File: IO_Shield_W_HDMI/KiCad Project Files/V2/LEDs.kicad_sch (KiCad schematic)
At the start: 70 parts, among them Q1 FDN340P, Q2 FDN340P, Q3 FDN340P, Q4 FDN340P, SW1 SW_DIP_x08, SW2 SW_DIP_x08

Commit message: working on placement
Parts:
- RN1, RN10, RN11, RN19, RN2, RN20, RN21, RN23, RN24, RN3, RN4, RN9: value R_Pack04 -> 1k
- RN13, RN14, RN15, RN16, RN17, RN22, RN7, RN8: value R_Pack04 -> 330
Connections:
- net AN2: no longer Q4.1 (G)
- net AFF0_B: now reaches RN7.8 (R1.2)
- net AFF0_B: now also AFF1.6 (b); no longer AFF1.1 (e)
- net AFF0_F: now reaches RN7.6 (R3.2)
- net AFF0_F: now also AFF1.9 (f); no longer AFF1.10 (g)
- net AFF0_D: now reaches AFF1.2 (d)
- net AFF0_D: now also RN5.7 (R2.2); no longer RN5.5 (R4.2)
- net AFF0_C: now reaches AFF1.4 (c), RN5.6 (R3.2)
- net AFF0_DP: now reaches AFF1.5 (DP)
- net AFF0_DP: now also RN5.5 (R4.2); no longer RN7.5 (R4.2)
- net AFF0_A: now reaches AFF1.7 (a)
- net AFF0_A: now also RN7.7 (R2.2); no longer RN5.8 (R1.2)
- net AFF1_B: now reaches RN8.8 (R1.2)
- net AFF1_B: now also AFF2.6 (b); no longer AFF2.1 (e)
- net AFF1_F: now reaches RN8.6 (R3.2)
- net AFF1_F: now also AFF2.9 (f); no longer AFF2.10 (g)
- net AFF1_D: now reaches AFF2.2 (d)
- net AFF1_D: now also RN6.7 (R2.2); no longer RN6.5 (R4.2)
- net AFF1_C: now reaches AFF2.4 (c), RN6.6 (R3.2)
- net AFF1_DP: now reaches AFF2.5 (DP)
- net AFF1_DP: now also RN6.5 (R4.2); no longer RN8.5 (R4.2)
- net AFF1_A: now reaches AFF2.7 (a)
- net AFF1_A: now also RN8.7 (R2.2); no longer RN6.8 (R1.2)
- net AFF2_B: now reaches RN13.8 (R1.2)
- net AFF2_B: now also AFF3.6 (b); no longer AFF3.1 (e)
- net AFF2_F: now reaches RN13.6 (R3.2)
- net AFF2_F: now also AFF3.9 (f); no longer AFF3.10 (g)
- net AFF2_D: now reaches AFF3.2 (d)
- net AFF2_D: now also RN12.7 (R2.2); no longer RN12.5 (R4.2)
- net AFF2_C: now reaches AFF3.4 (c), RN12.6 (R3.2)
- net AFF2_DP: now reaches AFF3.5 (DP)
- net AFF2_DP: now also RN12.5 (R4.2); no longer RN13.5 (R4.2)
- net AFF2_A: now reaches AFF3.7 (a)
- net AFF2_A: now also RN13.7 (R2.2); no longer RN12.8 (R1.2)
- net AFF3_DP: now reaches AFF4.5 (DP)
- net AFF3_DP: now also RN18.5 (R4.2); no longer RN22.5 (R4.2)
- net AFF3_F: now reaches RN22.6 (R3.2)
- net AFF3_F: now also AFF4.9 (f); no longer AFF4.10 (g)
- net AFF3_A: now reaches RN22.7 (R2.2)
- net AFF3_A: now also AFF4.7 (a); no longer AFF4.9 (f)
- net AFF3_B: now reaches RN22.8 (R1.2)
- net AFF3_B: now also AFF4.6 (b); no longer AFF4.1 (e)
- net AFF3_D: now reaches AFF4.2 (d)
- net AFF3_D: now also RN18.7 (R2.2); no longer RN18.5 (R4.2)
- net AFF3_C: now reaches AFF4.4 (c), RN18.6 (R3.2)
- net AFF3_E: now reaches RN18.8 (R1.2)
- net AFF3_E: now also AFF4.1 (e); no longer AFF4.7 (a)
- new net AFF0_E: AFF1.1 (e), RN5.8 (R1.2)
- new net AFF0_G: AFF1.10 (g), RN7.5 (R4.2)
- new net AFF1_E: AFF2.1 (e), RN6.8 (R1.2)
- new net AFF1_G: AFF2.10 (g), RN8.5 (R4.2)
- new net AFF2_E: AFF3.1 (e), RN12.8 (R1.2)
- new net AFF2_G: AFF3.10 (g), RN13.5 (R4.2)
- new net AFF3_G: AFF4.10 (g), RN22.5 (R4.2)
- new net AN3: Q4.1 (G)
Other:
- moved on the sheet: AFF1, AFF2, AFF3, AFF4, D1, D10, D11, D12, D13, D14, D15, D16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

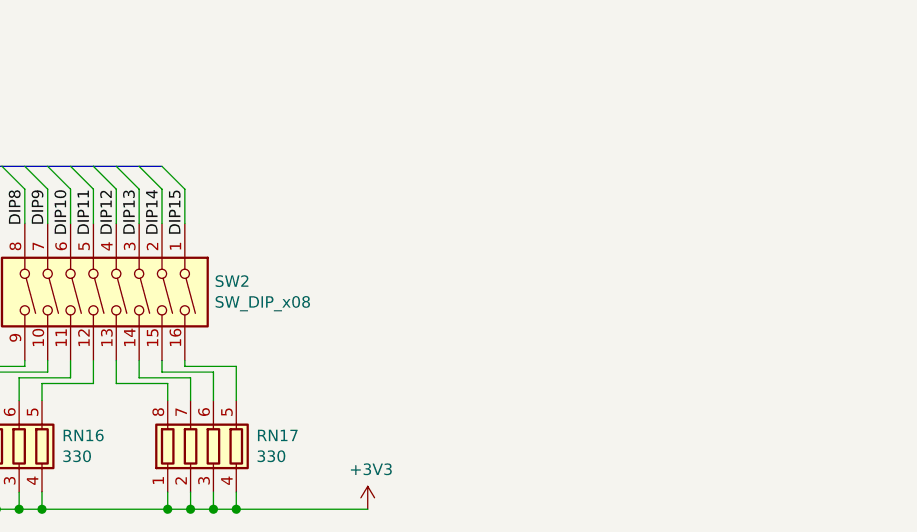
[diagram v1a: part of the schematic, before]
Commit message: switches and 7seg routed
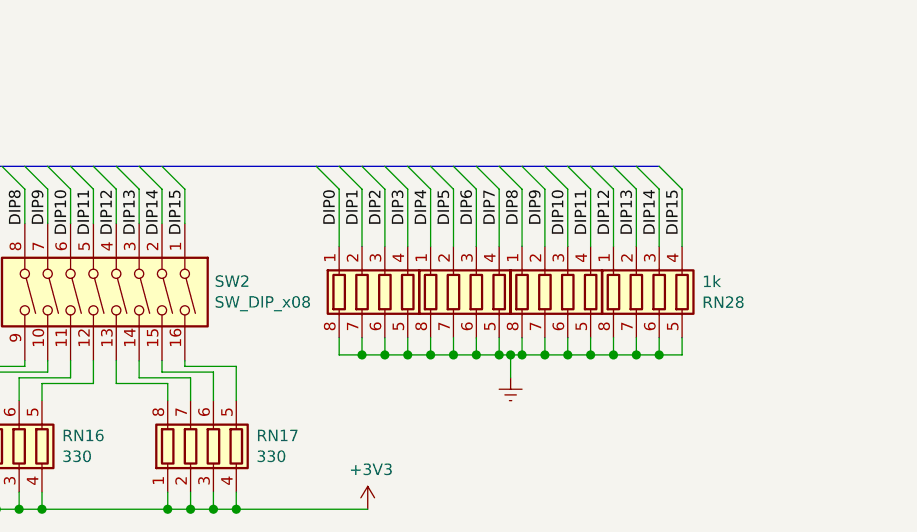
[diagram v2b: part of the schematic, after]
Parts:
- added RN25, RN26, RN27: 330, Resistor_SMD:R_Array_Convex_4x0603, symbol Device:R_Pack04
- added RN28: 1k, Resistor_SMD:R_Array_Convex_4x0603, symbol Device:R_Pack04
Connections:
- net DIP0: now also RN25.1 (R1.1)
- net DIP1: now also RN25.2 (R2.1)
- net DIP10: now also RN27.3 (R3.1)
- net DIP11: now also RN27.4 (R4.1)
- net DIP12: now also RN28.1 (R1.1)
- net DIP13: now also RN28.2 (R2.1)
- net DIP14: now also RN28.3 (R3.1)
- net DIP15: now also RN28.4 (R4.1)
- net DIP2: now also RN25.3 (R3.1)
- net DIP3: now also RN25.4 (R4.1)
- net DIP4: now also RN26.1 (R1.1)
- net DIP5: now also RN26.2 (R2.1)
- net DIP6: now also RN26.3 (R3.1)
- net DIP7: now also RN26.4 (R4.1)
- net DIP8: now also RN27.1 (R1.1)
- net DIP9: now also RN27.2 (R2.1)
- net GNDREF: now also RN25.5 (R4.2), RN25.6 (R3.2), RN25.7 (R2.2), RN25.8 (R1.2), RN26.5 (R4.2), RN26.6 (R3.2), RN26.7 (R2.2), RN26.8 (R1.2), RN27.5 (R4.2), RN27.6 (R3.2), RN27.7 (R2.2), RN27.8 (R1.2), RN28.5 (R4.2), RN28.6 (R3.2), RN28.7 (R2.2), RN28.8 (R1.2)
